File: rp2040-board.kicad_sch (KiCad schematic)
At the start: 92 parts, among them J1 24V IN, J10 E0-RUNOUT, J11 FAN0, J12 FAN1, J13 FAN2, J14 HB, J15 E0, J16 TH-E0, J2 USB4105-GF-A, J22 Exp. Header 2, J23 Exp. Header 3, J3 PGA2040, J4 Exp. Header 1, J5 PROBE, J6 X-ENDSTOP, J7 TH-HB, J8 Y-ENDSTOP, J9 Z-ENDSTOP, Q1 AO3400C, Q2 AO3400C, Q3 AO3400C, U1 AMS1117-3.3, U2 TPS5450DDAR, U3 74HCT365D,653, U4 FDS8896, U5 FDS8896

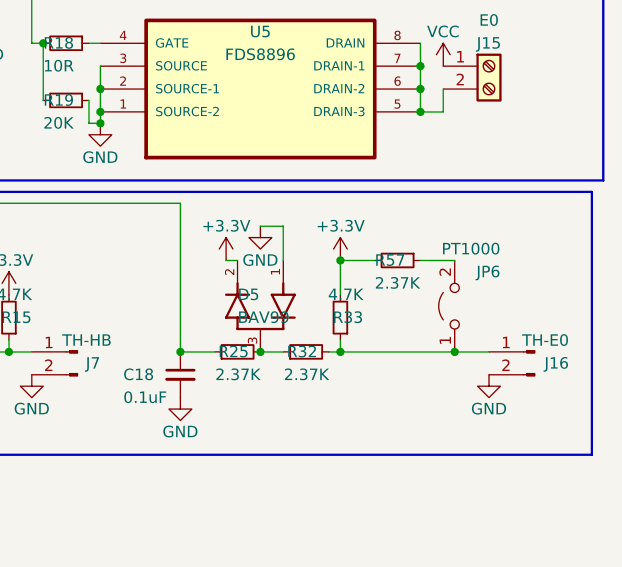
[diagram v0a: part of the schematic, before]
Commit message: Change Inductor & PT1000 Resistor
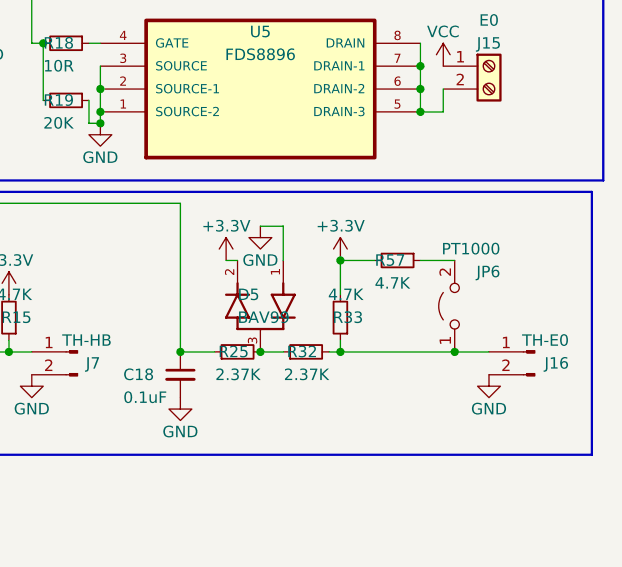
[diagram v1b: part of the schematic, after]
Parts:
- L1: MANUFACTURER Taiyo Yuden -> TDK
- R15, R33: MANUFACTURER YAGEO -> Panasonic
- R57: value 2.37K -> 4.7K; MANUFACTURER YAGEO -> Panasonic
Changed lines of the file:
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@@
       (effects (font (size 1.27 1.27)) hide)
     )
-    (property "Datasheet" "https://datasheet.lcsc.com/lcsc/2010201810_YAGEO-RT0805CRE074K7L_C706301.pdf" (id 3) (at 184.15 154.94 0)
+    (property "Datasheet" "https://datasheet.lcsc.com/lcsc/2004071032_PANASONIC-ERA6AEB472V_C473295.pdf" (id 3) (at 184.15 154.94 0)
       (effects (font (size 1.27 1.27)) hide)
     )
-    (property "MANUFACTURER" "YAGEO" (id 4) (at 184.15 154.94 0)
+    (property "MANUFACTURER" "Panasonic" (id 4) (at 184.15 154.94 0)
       (effects (font (size 1.27 1.27)) hide)
     )
@@
       (effects (font (size 1.27 1.27)) hide)
     )
-    (property "Datasheet" "https://ds.yuden.co.jp/TYCOMPAS/ut/detail?pn=LBC3225T150KR%20%20&u=M" (id 3) (at 110.49 171.45 0)
+    (property "Datasheet" "https://datasheet.lcsc.com/lcsc/1810201252_TDK-NLCV32T-150K-PF_C250186.pdf" (id 3) (at 110.49 171.45 0)
       (effects (font (size 1.27 1.27)) hide)
     )
-    (property "MANUFACTURER" "Taiyo Yuden" (id 4) (at 110.49 171.45 0)
+    (property "MANUFACTURER" "TDK" (id 4) (at 110.49 171.45 0)
       (effects (font (size 1.27 1.27)) hide)
     )
@@
       (effects (font (size 1.27 1.27)) hide)
     )
-    (property "Datasheet" "https://datasheet.lcsc.com/lcsc/2010201810_YAGEO-RT0805CRE074K7L_C706301.pdf" (id 3) (at 220.98 154.94 0)
+    (property "Datasheet" "https://datasheet.lcsc.com/lcsc/2004071032_PANASONIC-ERA6AEB472V_C473295.pdf" (id 3) (at 220.98 154.94 0)
       (effects (font (size 1.27 1.27)) hide)
     )
-    (property "MANUFACTURER" "YAGEO" (id 4) (at 220.98 154.94 0)
+    (property "MANUFACTURER" "Panasonic" (id 4) (at 220.98 154.94 0)
       (effects (font (size 1.27 1.27)) hide)
     )
@@
       (effects (font (size 1.27 1.27)) (justify left))
     )
-    (property "Value" "2.37K" (id 1) (at 224.79 151.13 90)
+    (property "Value" "4.7K" (id 1) (at 224.79 151.13 90)
       (effects (font (size 1.27 1.27)) (justify left))
     )
@@
       (effects (font (size 1.27 1.27)) hide)
     )
-    (property "Datasheet" "https://datasheet.lcsc.com/lcsc/2010201810_YAGEO-RT0805CRE074K7L_C706301.pdf" (id 3) (at 227.33 148.59 0)
+    (property "Datasheet" "https://datasheet.lcsc.com/lcsc/2004071032_PANASONIC-ERA6AEB472V_C473295.pdf" (id 3) (at 227.33 148.59 0)
       (effects (font (size 1.27 1.27)) hide)
     )
-    (property "MANUFACTURER" "YAGEO" (id 4) (at 227.33 148.59 0)
+    (property "MANUFACTURER" "Panasonic" (id 4) (at 227.33 148.59 0)
       (effects (font (size 1.27 1.27)) hide)
     )
@@
     )
     (path "/f780f133-240d-4f29-a274-8668016773e8"
-      (reference "R57") (unit 1) (value "2.37K") (footprint "Resistor_SMD:R_0805_2012Metric_Pad1.20x1.40mm_HandSolder")
+      (reference "R57") (unit 1) (value "4.7K") (footprint "Resistor_SMD:R_0805_2012Metric_Pad1.20x1.40mm_HandSolder")
     )
     (path "/5734cfa1-2e82-405b-aa6a-9b651f522acf"

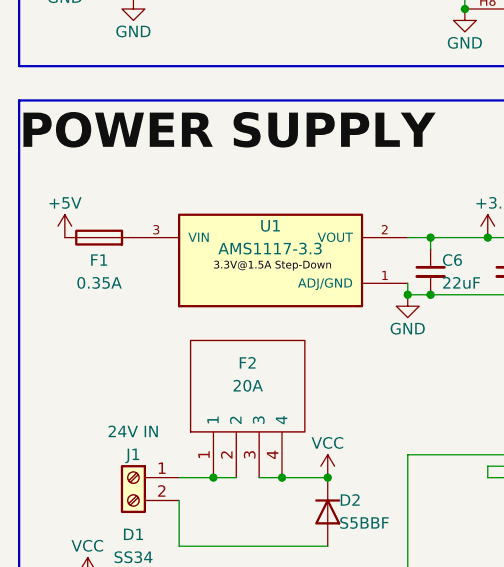
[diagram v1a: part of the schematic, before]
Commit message: Update BOM + Minor PCB Touchups
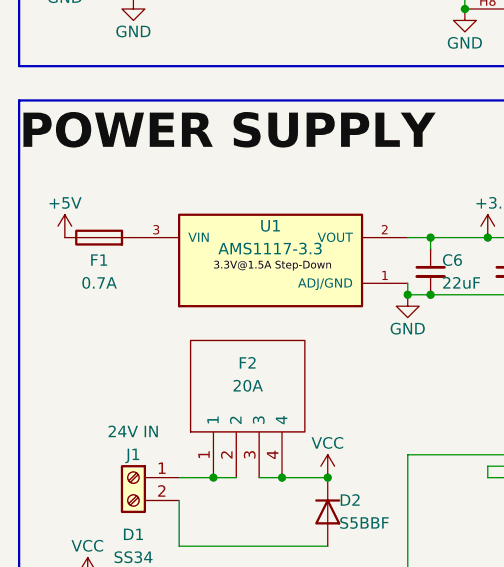
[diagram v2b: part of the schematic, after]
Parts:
- F1: value 0.35A -> 0.7A; MANUFACTURER YAGEO -> BNstar
- F2: MANUFACTURER Littelfuse -> DEALON
- J22, J23, J4: MANUFACTURER (none) -> HCTL
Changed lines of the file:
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@@
       (effects (font (size 1.27 1.27)) hide)
     )
-    (property "Datasheet" "~" (id 3) (at 30.48 39.37 0)
+    (property "Datasheet" "https://datasheet.lcsc.com/lcsc/2109151430_HCTL-PZ254-1-02-Z-8-5_C2894925.pdf" (id 3) (at 30.48 39.37 0)
+      (effects (font (size 1.27 1.27)) hide)
+    )
+    (property "MANUFACTURER" "HCTL" (id 4) (at 30.48 39.37 0)
       (effects (font (size 1.27 1.27)) hide)
     )
@@
       (effects (font (size 1.27 1.27)) hide)
     )
-    (property "Datasheet" "~" (id 3) (at 30.48 29.21 0)
+    (property "Datasheet" "https://datasheet.lcsc.com/lcsc/2109151430_HCTL-PZ254-1-02-Z-8-5_C2894925.pdf" (id 3) (at 30.48 29.21 0)
+      (effects (font (size 1.27 1.27)) hide)
+    )
+    (property "MANUFACTURER" "HCTL" (id 4) (at 30.48 29.21 0)
       (effects (font (size 1.27 1.27)) hide)
     )
@@
       (effects (font (size 1.27 1.27)) (justify left) hide)
     )
-    (property "Datasheet" "https://m.littelfuse.com/~/media/electronics/datasheets/fuse_clips/littelfuse_fuseclip_100_datasheet.pdf.pdf" (id 3) (at 35.56 162.56 0)
+    (property "Datasheet" "https://datasheet.lcsc.com/lcsc/2201121700_DEALON-BX505-33_C2935870.pdf" (id 3) (at 35.56 162.56 0)
       (effects (font (size 1.27 1.27)) (justify left) hide)
     )
-    (property "MANUFACTURER" "Littelfuse" (id 4) (at 35.56 179.07 0)
+    (property "MANUFACTURER" "DEALON" (id 4) (at 35.56 179.07 0)
       (effects (font (size 1.27 1.27)) hide)
     )
@@
     (in_bom yes) (on_board yes)
     (property "Reference" "F1" (id 0) (at 22.86 154.94 90))
-    (property "Value" "0.35A" (id 1) (at 22.86 157.48 90))
+    (property "Value" "0.7A" (id 1) (at 22.86 157.48 90))
     (property "Footprint" "Fuse:Fuse_1812_4532Metric_Pad1.30x3.40mm_HandSolder" (id 2) (at 22.86 154.178 90)
       (effects (font (size 1.27 1.27)) hide)
     )
-    (property "Datasheet" "https://www.digikey.com/en/products/detail/yageo/SMD1812B035TF-30/10126705" (id 3) (at 22.86 152.4 0)
-      (effects (font (size 1.27 1.27)) hide)
-    )
-    (property "MANUFACTURER" "YAGEO" (id 4) (at 22.86 152.4 0)
+    (property "Datasheet" "https://datasheet.lcsc.com/lcsc/2103221808_BNstar-SMD1812-035C-30V_C2760286.pdf" (id 3) (at 22.86 152.4 0)
+      (effects (font (size 1.27 1.27)) hide)
+    )
+    (property "MANUFACTURER" "BNstar" (id 4) (at 22.86 152.4 0)
       (effects (font (size 1.27 1.27)) hide)
     )
@@
       (effects (font (size 1.27 1.27)) hide)
     )
-    (property "Datasheet" "~" (id 3) (at 30.48 49.53 0)
+    (property "Datasheet" "https://datasheet.lcsc.com/lcsc/2109151430_HCTL-PZ254-1-02-Z-8-5_C2894925.pdf" (id 3) (at 30.48 49.53 0)
+      (effects (font (size 1.27 1.27)) hide)
+    )
+    (property "MANUFACTURER" "HCTL" (id 4) (at 30.48 49.53 0)
       (effects (font (size 1.27 1.27)) hide)
     )
@@
     )
     (path "/b12654e8-5f27-4d97-bb63-394a1226df0a"
-      (reference "F1") (unit 1) (value "0.35A") (footprint "Fuse:Fuse_1812_4532Metric_Pad1.30x3.40mm_HandSolder")
+      (reference "F1") (unit 1) (value "0.7A") (footprint "Fuse:Fuse_1812_4532Metric_Pad1.30x3.40mm_HandSolder")
     )
     (path "/7d8543f6-406c-45ca-a698-ed0b16e474d8"

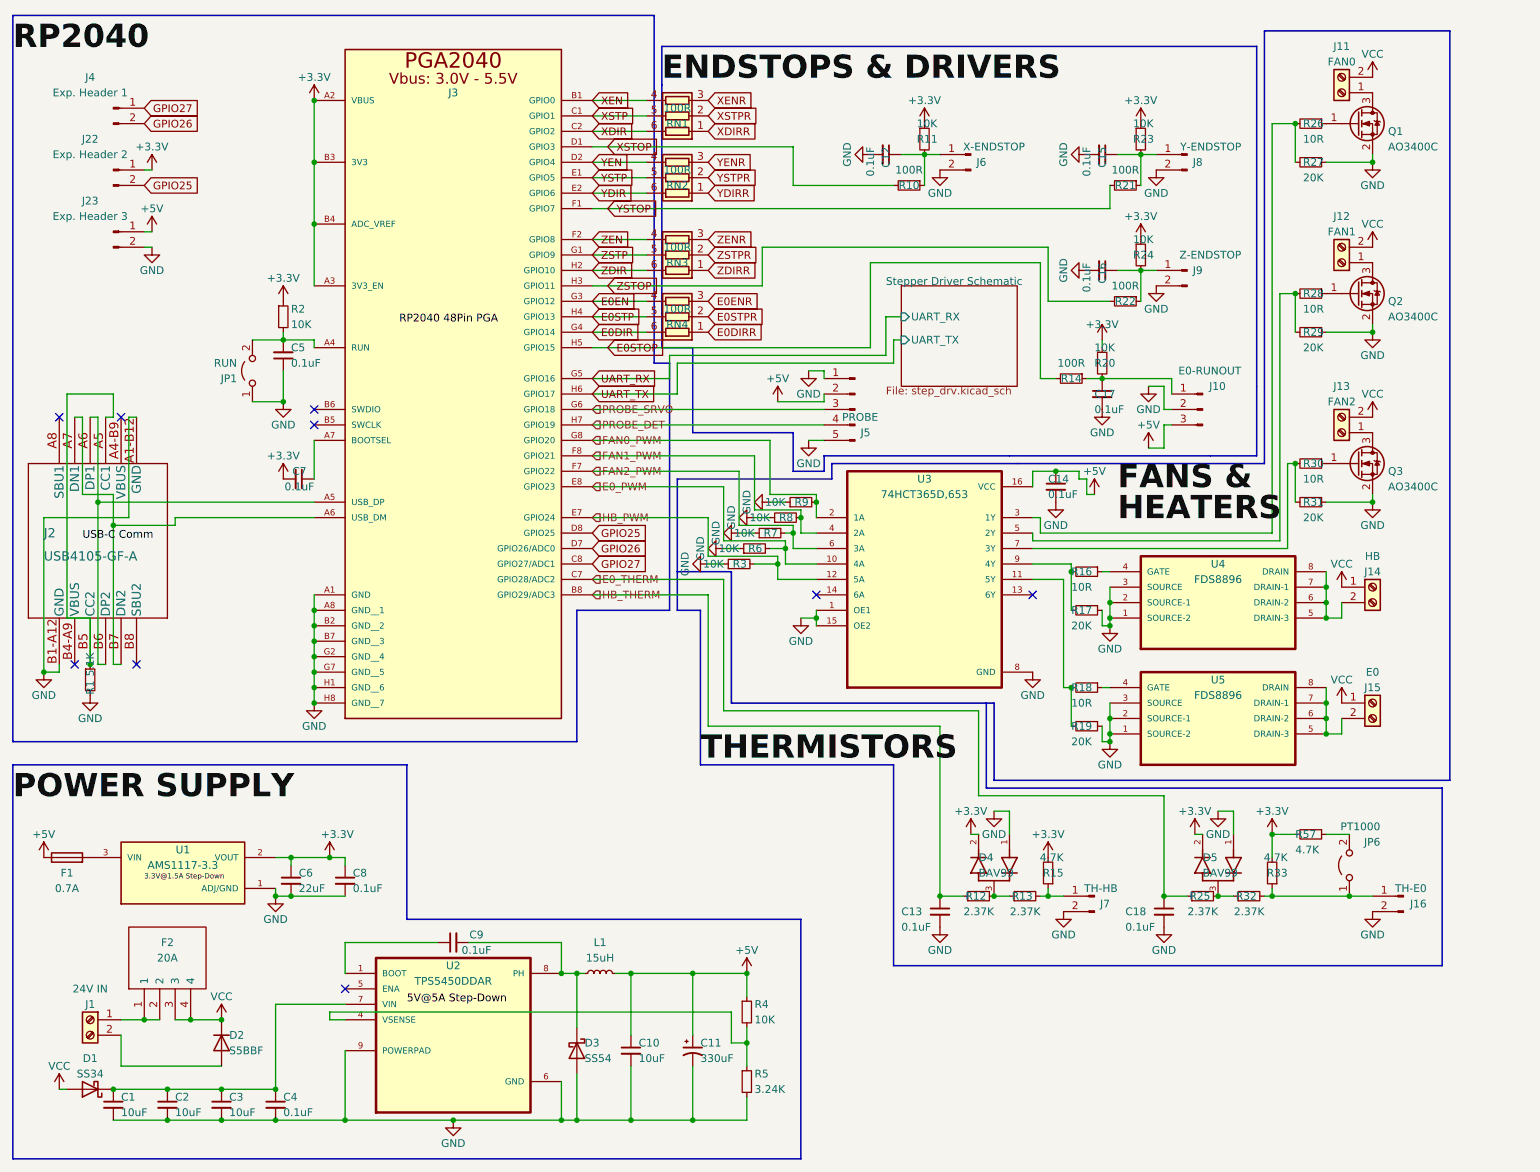
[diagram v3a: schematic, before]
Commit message: add fan diodes + cleanup + copper fill clearances
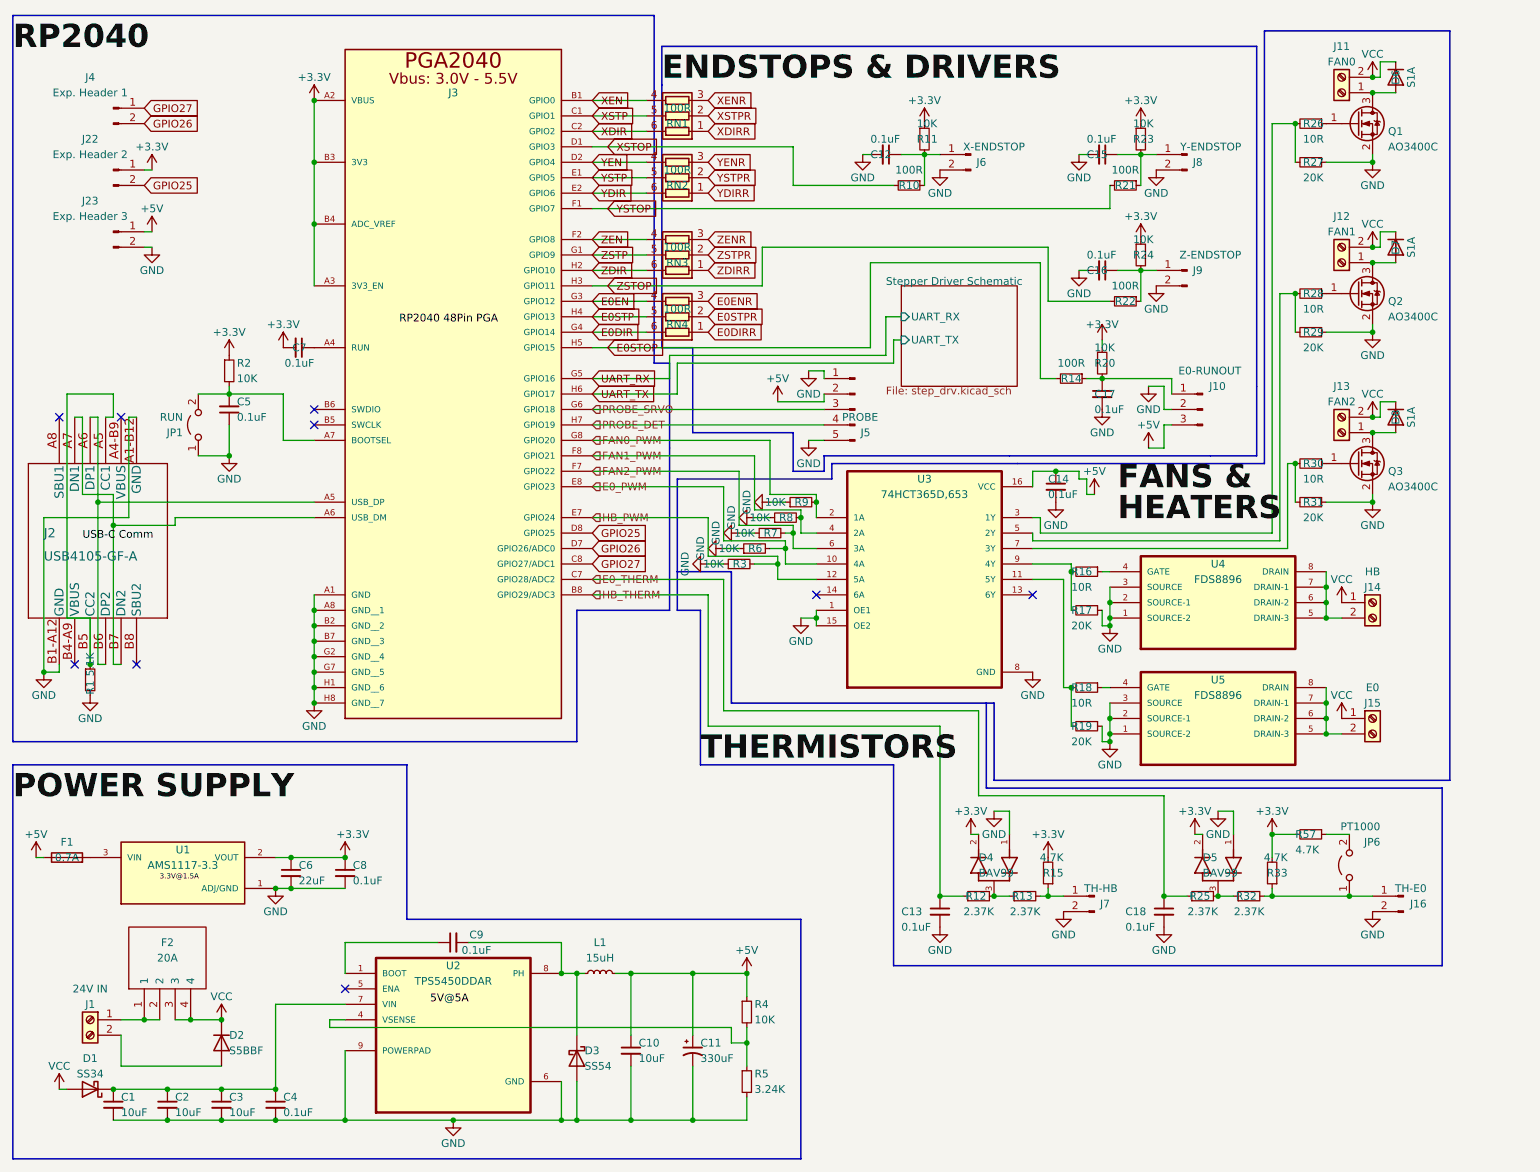
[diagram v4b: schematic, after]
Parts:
- added D6, D7, D8: S1A, Diode_SMD:D_SMA, symbol Diode:1N4007
- C1, C10, C12, C13, C14, C15, C16, C17, C18, C2, C3, C4, C5, C6, C7, C8, C9: footprint Capacitor_SMD:C_0805_2012Metric_Pad1.18x1.45mm_HandSolder -> Capacitor_SMD:C_0805_2012Metric_Pad1.18x1.45mm
- D1, D3: footprint Diode_SMD:D_SMA_Handsoldering -> Diode_SMD:D_SMA
- D2: footprint Diode_SMD:D_SMB_Handsoldering -> Diode_SMD:D_SMB
- F1: footprint Fuse:Fuse_1812_4532Metric_Pad1.30x3.40mm_HandSolder -> Fuse:Fuse_1812_4532Metric_Pad1.30x3.40mm
- F2: footprint 01000063Z -> 01000063Z:01000063Z
- L1: footprint Inductor_SMD:L_1210_3225Metric_Pad1.42x2.65mm_HandSolder -> Inductor_SMD:L_1210_3225Metric_Pad1.42x2.65mm
- Q1, Q2, Q3: footprint Package_TO_SOT_SMD:SOT-23_Handsoldering -> Package_TO_SOT_SMD:SOT-23
- R1, R10, R11, R12, R13, R14, R15, R16, R17, R18, R19, R2, R20, R21, R22, R23, R24, R25, R26, R27, R28, R29, R3, R30, R31, R32, R33, R4, R5, R57, R6, R7, R8, R9: footprint Resistor_SMD:R_0805_2012Metric_Pad1.20x1.40mm_HandSolder -> Resistor_SMD:R_0805_2012Metric_Pad1.20x1.40mm
- U1: footprint SOT229P700X180-4N -> AMS1117-3.3:SOT229P700X180-4N
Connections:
- net VCC: now also D6.1 (K), D7.1 (K), D8.1 (K)
- net at J11.1 (Pin_1), Q1.3 (D): now also D6.2 (A)
- net at J12.1 (Pin_1), Q2.3 (D): now also D7.2 (A)
- net at C7.1: now also J3.A4 (RUN); no longer J3.A7 (BOOTSEL)
- net at J13.1 (Pin_1), Q3.3 (D): now also D8.2 (A)
- net at C5.2, JP1.2 (B), R2.2: now also J3.A7 (BOOTSEL); no longer J3.A4 (RUN)
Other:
- moved on the sheet: C6, C8, D3, J14, J15
